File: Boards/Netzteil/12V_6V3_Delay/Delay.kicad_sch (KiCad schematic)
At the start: 47 parts, among them J2 Standby, J3 Standby, J4 Conn_01x03, J5 Standby, P10 Relais, P11 Relais, P9 Relais, Q3 BS170, Q4 BS170, Q5 BC337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

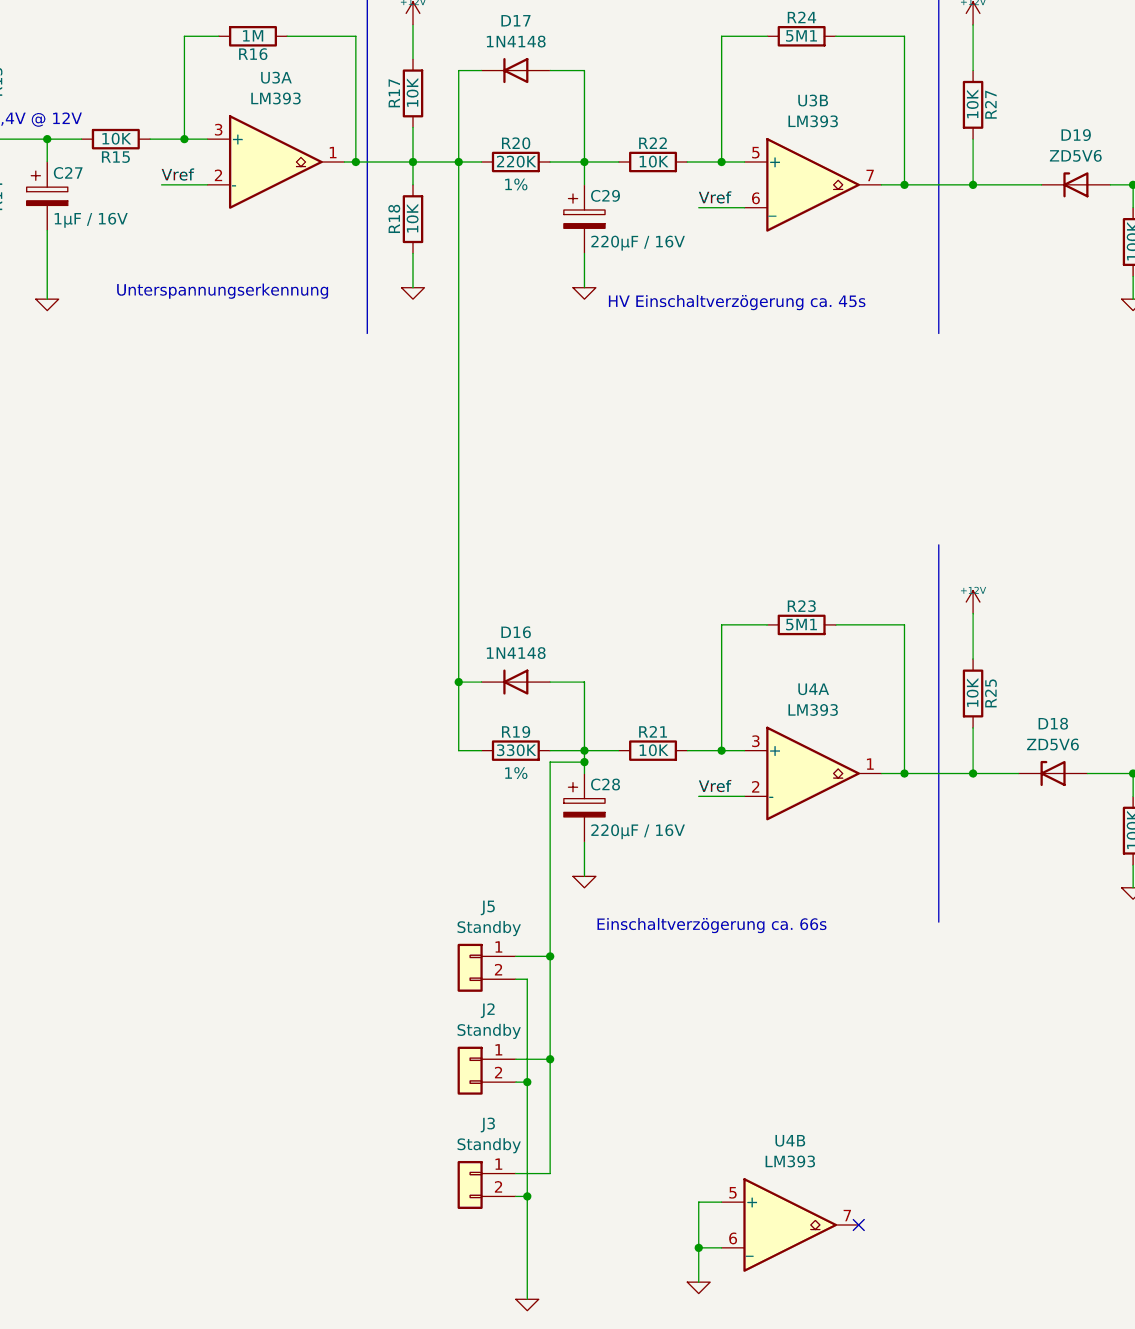
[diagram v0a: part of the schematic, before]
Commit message: 6.3V, 400V und 400V Regler Boards bestellt
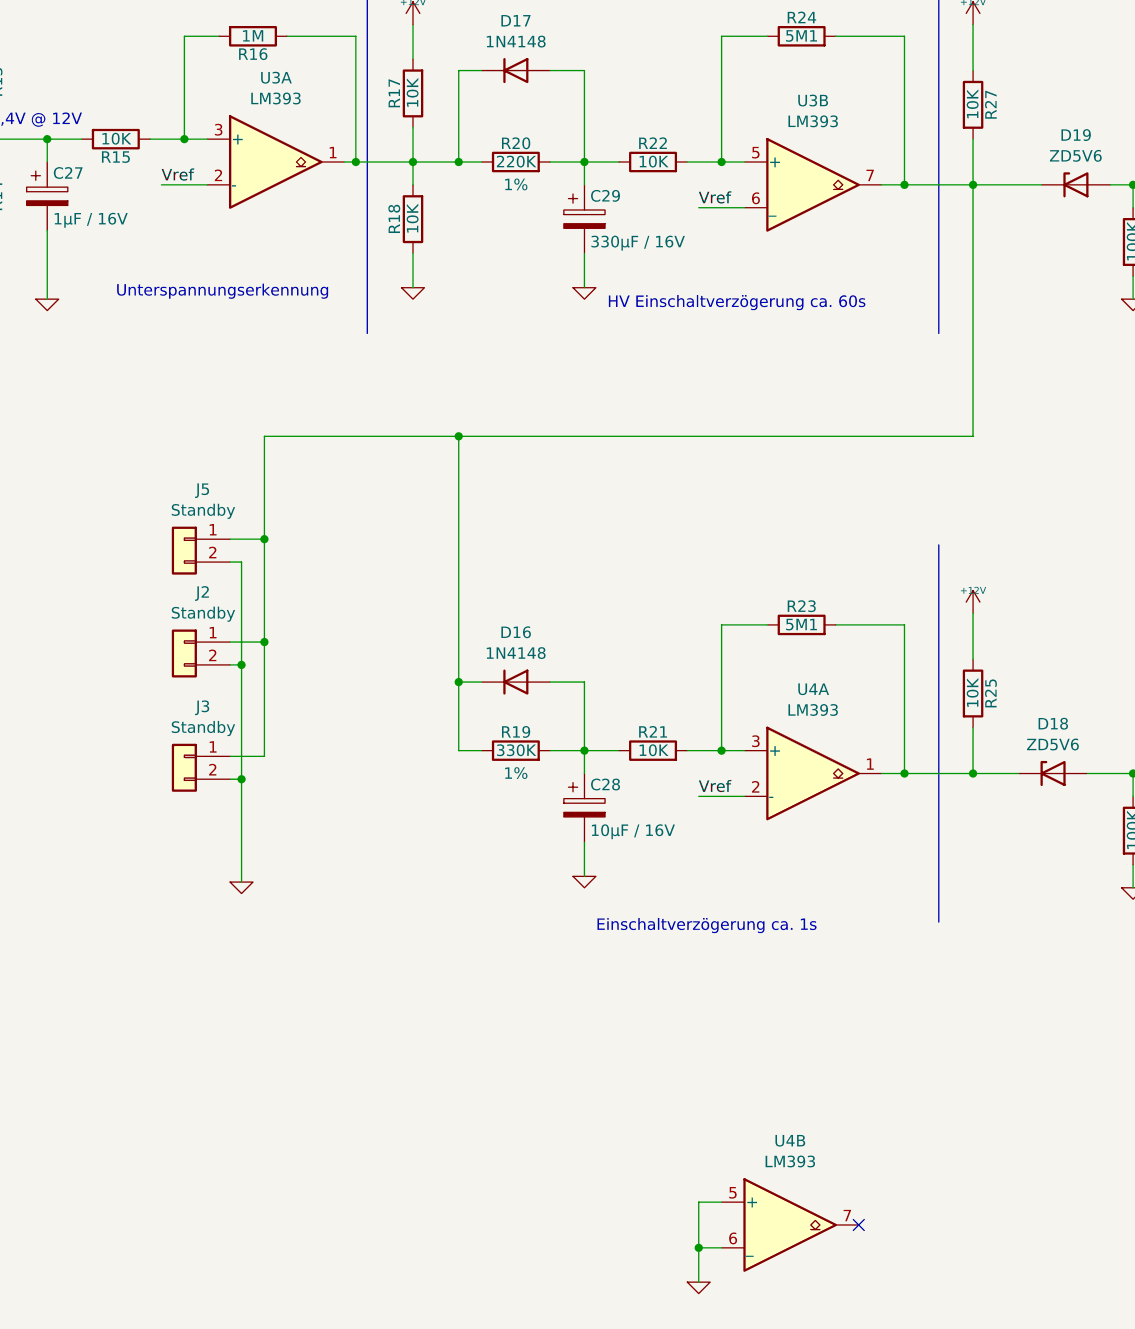
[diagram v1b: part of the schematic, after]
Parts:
- C24, C25, C26: footprint Capacitor_THT:C_Disc_D3.0mm_W2.0mm_P2.50mm -> Capacitor_THT:C_Disc_D4.3mm_W1.9mm_P5.00mm
- C27: footprint Capacitor_THT:CP_Radial_D5.0mm_P2.00mm -> Capacitor_THT:CP_Radial_D4.0mm_P1.50mm
- C28: value 220µF / 16V -> 10µF / 16V; footprint Capacitor_THT:CP_Radial_D8.0mm_P3.50mm -> Capacitor_THT:CP_Radial_D5.0mm_P2.00mm
- C29: value 220µF / 16V -> 330µF / 16V; footprint Capacitor_THT:CP_Radial_D8.0mm_P3.50mm -> Capacitor_THT:CP_Radial_D8.0mm_P5.00mm
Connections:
- net at D17.1 (K), R16.1, R17.1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: no longer D16.1 (K), R19.1
- net at D19.1 (K), R24.2, R27.2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: now also D16.1 (K), J2.1 (Pin_1), J3.1 (Pin_1), J5.1 (Pin_1), R19.1
- net at C28.1, D16.2 (A), R19.2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: no longer J2.1 (Pin_1), J3.1 (Pin_1), J5.1 (Pin_1)
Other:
- note added: "Einschaltverzögerung ca. 1s"
- note added: "HV Einschaltverzögerung ca. 60s"
- note removed: "Einschaltverzögerung ca. 66s"
- note removed: "HV Einschaltverzögerung ca. 45s"
- moved on the sheet: J2, J3, J5
